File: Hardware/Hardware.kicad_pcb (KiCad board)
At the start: 2 copper layers, 39 parts, among them J2 RJ45_LED_Shielded, J3 USB_A, J5 Conn_01x06_Pin, SW1 SW_SPST, SW14 SW_Push, SW2 SW_Push, SW3 SW_Push, SW4 SW_Push, SW5 SW_Push, SW6 SW_Push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

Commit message: Added some traces
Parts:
- moved D14 15.7 mm to (249.4, 87.0)
- moved SW1 9.99 mm to (249.2, 101.1)
- moved Conn1 6.48 mm to (167.4, 78.4)
- moved R1 5.87 mm to (238.0, 101.6), turned to 180 degrees
- moved R9 3.01 mm to (223.1, 103.1)
- moved BT1 2.03 mm to (236.7, 132.5)
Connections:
- SW2 pad 1: +3.3V -> +3V3
- SW3 pad 1: +3.3V -> +3V3
- SW4 pad 1: +3.3V -> +3V3
- SW5 pad 1: +3.3V -> +3V3
- SW6 pad 1: +3.3V -> +3V3
- SW7 pad 1: +3.3V -> +3V3
- U7 pad 4: +3.3V -> +3V3
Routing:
- net +3V3: track 0.00 -> 238.6 mm, vias 0 -> 4
- net kp_button6: track 0.00 -> 95.8 mm, vias 0 -> 1
- net MISO: track 0.00 -> 73.1 mm, vias 0 -> 1
- net kp_button4: track 0.00 -> 70.7 mm, vias 0 -> 1
- net kp_button5: track 0.00 -> 69.5 mm, vias 0 -> 1
- net MOSI: track 0.00 -> 66.1 mm, vias 0 -> 1
- net +5V: track 0.00 -> 62.1 mm, vias 0 -> 1
- net kp_button3: track 0.00 -> 61.8 mm, vias 0 -> 1
- net T_CS: track 0.00 -> 61.5 mm
- net SCK: track 0.00 -> 51.8 mm, vias 0 -> 1
- net kp_button1: track 0.00 -> 50.3 mm, vias 0 -> 1
- net Rx+: track 0.00 -> 46.6 mm, vias 0 -> 1
- net Rx-: track 0.00 -> 46.6 mm, vias 0 -> 1
- net T_IRQ: track 0.00 -> 46.2 mm, vias 0 -> 1
- net LED: track 0.00 -> 44.9 mm
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- added copper zone on B.Cu, net GND
- added copper zone on F.Cu, net GND
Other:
- board outline added: 102.9 x 121.9 mm

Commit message: finished up the layout and cleaned up libraries
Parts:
- removed C7: 0.1uF, Capacitor_SMD:C_0603_1608Metric_Pad1.08x0.95mm_HandSolder
- removed C8: 1uF, Capacitor_SMD:C_0603_1608Metric_Pad1.08x0.95mm_HandSolder
- added C5: 4.7nF, Capacitor_SMD:C_0603_1608Metric_Pad1.08x0.95mm_HandSolder, F.Cu at (177.1, 74.2)
- added H1: MountingHole, MRDT_Drill_Holes:4_40_Hole, F.Cu at (241.0, 65.0)
- added H2: MountingHole, MRDT_Drill_Holes:4_40_Hole, F.Cu at (157.7, 65.0)
- added H3: MountingHole, MRDT_Drill_Holes:4_40_Hole, F.Cu at (241.0, 130.6)
- added H4: MountingHole, MRDT_Drill_Holes:4_40_Hole, F.Cu at (157.8, 130.5)
- added H5: MountingHole, MRDT_Drill_Holes:4_40_Hole, F.Cu at (166.9, 196.6)
- added H6: MountingHole, MRDT_Drill_Holes:4_40_Hole, F.Cu at (231.9, 196.6)
- C6: value 4.7nF -> 1uF
- D1: value D_Schottky -> D_Schottky_ZLLS500; footprint MRDT_Passives:SOT-23_Diode -> Tester:D_Schottky_ZLLS500
- D2: renamed from D15; value D_Schottky -> D_Schottky_ZLLS500; footprint MRDT_Passives:SOT-23_Diode -> Tester:D_Schottky_ZLLS500
- SW2, SW3, SW4, SW5, SW6, SW7: footprint Button_Switch_SMD:SW_SPST_TL3305A -> Tester:SW_SPST_TL3301
- U7: footprint sw_spst:DISPLAY_ILI9341_TOUCH_32 -> Tester:DISPLAY_ILI9341_TOUCH_32
- moved SW1 94.0 mm to (157.2, 81.6), turned to -90 degrees
- moved D3 92.5 mm to (157.5, 97.2), turned to -90 degrees
- moved R4 85.3 mm to (157.5, 93.3), turned to 90 degrees
- moved BT1 69.0 mm to (168.7, 121.4)
- moved R9 50.3 mm to (174.8, 116.8), turned to 90 degrees
- moved R8 47.9 mm to (177.2, 77.7), turned to 180 degrees
- moved SW2 42.6 mm to (170.2, 156.5), turned to 0 degrees
- moved SW7 38.6 mm to (225.3, 160.0), turned to 0 degrees
- moved C2 34.5 mm to (165.7, 111.5), turned to 180 degrees
- moved SW3 33.8 mm to (184.2, 164.1), turned to 0 degrees
- moved R2 32.1 mm to (182.8, 77.7)
- moved C3 31.1 mm to (170.1, 111.5)
- moved C4 28.4 mm to (182.9, 74.2), turned to 180 degrees
- moved SW4 28.1 mm to (207.5, 160.0), turned to 0 degrees
- moved C6 28.1 mm to (172.0, 116.8), turned to -90 degrees
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- renumbered D14 to D3, SW14 to SW8
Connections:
- net kp_button1 renamed KP_ACCEPT
- net kp_button2 renamed KP_BACK
- net kp_button3 renamed KP_RIGHT
- net kp_button6 renamed KP_LEFT
- C6 pad 1: Net-(C6-Pad1) -> WiFi_EN
- D1 pad 2: Net-(D1-A) -> unconnected-(D1-NC-Pad2)
- D1 pad 3: (no net) -> Net-(D1-A)
- D2 pad 2: Net-(D15-A) -> unconnected-(D2-NC-Pad2)
- D2 pad 3: (no net) -> Net-(D2-A)
- J3 pad 1: Net-(D15-A) -> Net-(D2-A)
- R8 pad 2: Net-(C6-Pad1) -> Net-(C5-Pad1)
- SW2 pad 1: +3V3 -> GND
- SW3 pad 1: +3V3 -> GND
- SW4 pad 1: +3V3 -> GND
- SW5 pad 1: +3V3 -> GND
- SW5 pad 2: kp_button4 -> KP_UP
- SW6 pad 1: +3V3 -> GND
- SW6 pad 2: kp_button5 -> KP_DOWN
- SW7 pad 1: +3V3 -> GND
- U3 pad 17: kp_button4 -> KP_DOWN
- U3 pad 18: kp_button5 -> KP_UP
- U3 pad 33: unconnected-(U3-MCLK2-Pad33) -> WiFi_EN
- U3 pad D-: (no net) -> USB_D-
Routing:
- net +5V: track 62.1 -> 167.5 mm, vias 1 -> 4
- net +3V3: track 238.6 -> 151.2 mm
- net KP_DOWN: track 0.00 -> 83.3 mm, vias 0 -> 1
- net Net-(D1-A): track 21.4 -> 96.8 mm
- net kp_button4: track 70.7 -> 0.00 mm, vias 1 -> 0
- net kp_button5: track 69.5 -> 0.00 mm, vias 1 -> 0
- net KP_UP: track 0.00 -> 68.2 mm, vias 0 -> 1
- net SCK: track 51.8 -> 94.6 mm, vias 1 -> 4
- net KP_ACCEPT: track 50.3 -> 91.2 mm
- net KP_BACK: track 43.9 -> 83.6 mm
- net WiFi_EN: track 34.1 -> 73.5 mm, vias 2 -> 0
- net MOSI: track 66.1 -> 104.3 mm, vias 1 -> 4
- net Net-(U2-CANH): track 17.0 -> 53.9 mm
- net Net-(U2-CANL): track 18.1 -> 52.8 mm
- net MISO: track 73.1 -> 96.9 mm, vias 1 -> 3
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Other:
- board size 102.9 x 121.9 mm -> 91.4 x 139.7 mm
- board text added: "Accept"
- board text added: "Back"

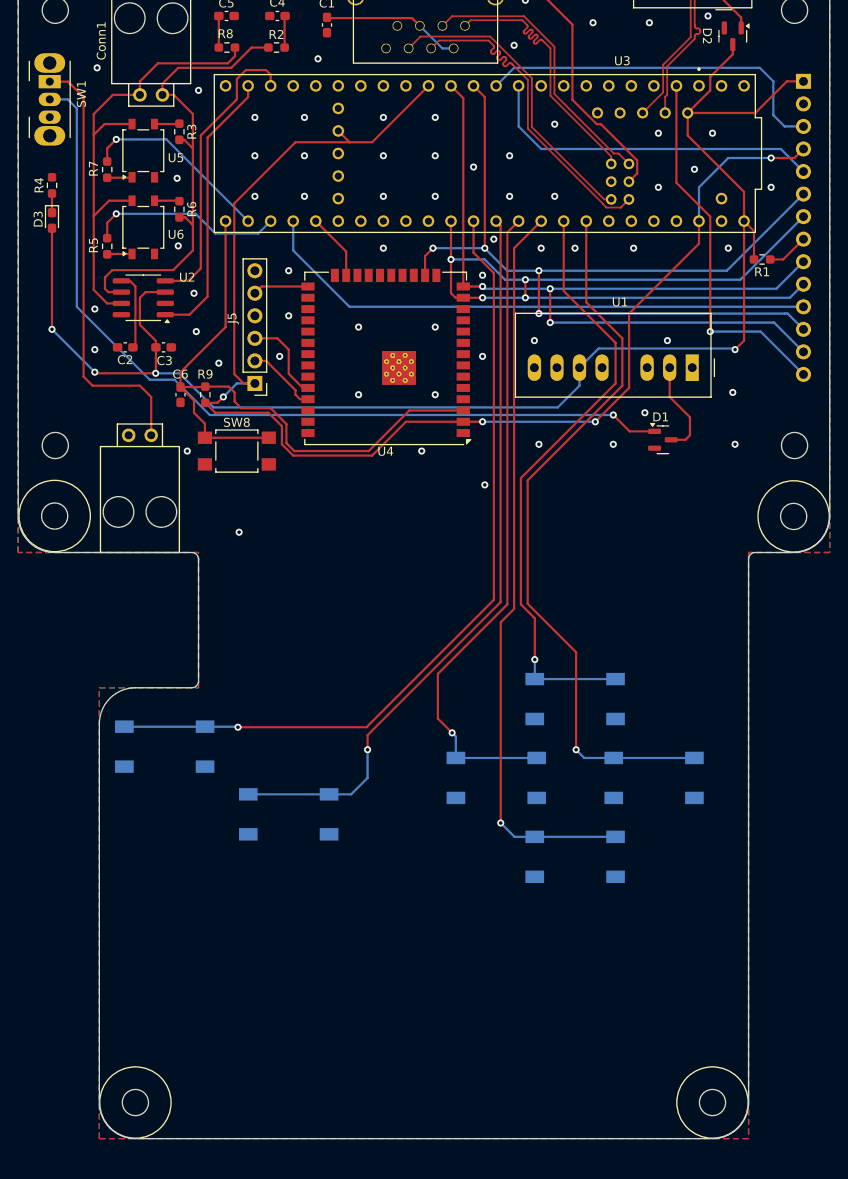
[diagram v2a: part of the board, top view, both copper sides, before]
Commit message: swapped buck and esp32 to make traces shorter
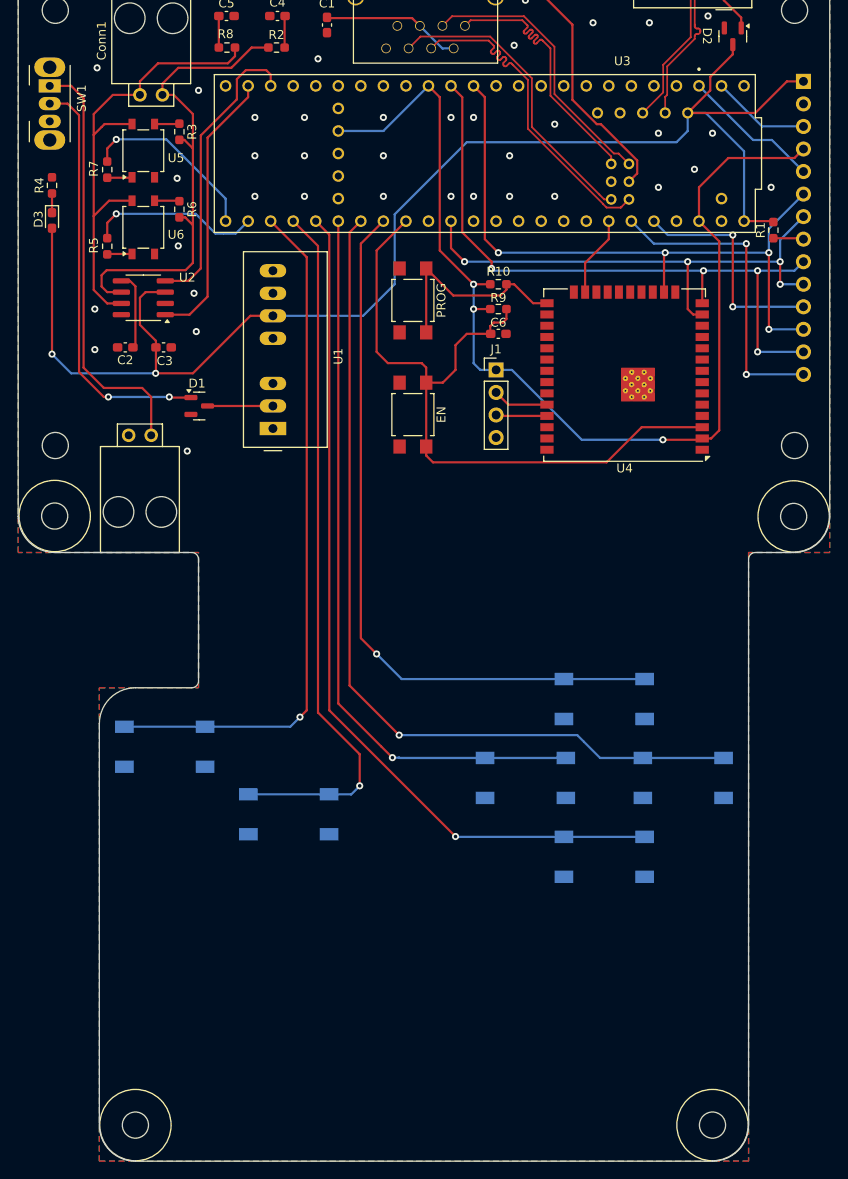
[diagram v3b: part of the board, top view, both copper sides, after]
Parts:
- removed J5: Conn_01x06_Pin, Connector_PinHeader_2.54mm:PinHeader_1x06_P2.54mm_Vertical
- added J1: Conn_01x04_Pin, Connector_PinHeader_2.54mm:PinHeader_1x04_P2.54mm_Vertical, F.Cu at (207.5, 114.0)
- added PROG: SW_Push, Button_Switch_SMD:SW_SPST_TL3305A, F.Cu at (198.1, 106.2)
- added R10: 10k, Resistor_SMD:R_0603_1608Metric_Pad0.98x0.95mm_HandSolder, F.Cu at (207.8, 104.4)
- moved D1 52.4 mm to (174.1, 118.1)
- moved U1 47.7 mm to (182.4, 120.7), turned to 90 degrees
- moved C6 36.5 mm to (207.8, 110.0), turned to 0 degrees
- moved R9 34.4 mm to (207.8, 107.2), turned to 0 degrees
- moved U4 27.0 mm to (222.0, 114.6)
- moved EN 20.3 mm to (198.1, 119.1), turned to -90 degrees
- moved R1 3.54 mm to (238.8, 98.3), turned to 90 degrees
- moved SW4 3.28 mm to (210.8, 160.0)
- moved SW5 3.28 mm to (219.7, 151.1)
- moved SW6 3.28 mm to (219.7, 168.9)
- moved SW7 3.28 mm to (228.6, 160.0)
- moved H5 2.54 mm to (166.9, 199.1)
- moved H6 2.54 mm to (231.9, 199.1)
- moved SW1 0.48 mm to (157.2, 82.0)
- renumbered SW8 to EN
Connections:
- U3 pad 0: unconnected-(U3-RX1-Pad0) -> LCD_CS
- U3 pad 1: unconnected-(U3-TX1-Pad1) -> DC
- U3 pad 10: LCD_CS -> unconnected-(U3-CS1-Pad10)
- U3 pad 14: KP_ACCEPT -> unconnected-(U3-A0-Pad14)
- U3 pad 15: KP_BACK -> unconnected-(U3-A1-Pad15)
- U3 pad 16: KP_RIGHT -> unconnected-(U3-A2-Pad16)
- U3 pad 17: KP_DOWN -> unconnected-(U3-A3-Pad17)
- U3 pad 18: KP_UP -> unconnected-(U3-A4-Pad18)
- U3 pad 19: KP_LEFT -> unconnected-(U3-A5-Pad19)
- U3 pad 2: T_IRQ -> unconnected-(U3-OUT2-Pad2)
- U3 pad 20: unconnected-(U3-A6-Pad20) -> WiFi_CS
- U3 pad 21: unconnected-(U3-A7-Pad21) -> T_IRQ
- U3 pad 22: unconnected-(U3-A8-Pad22) -> T_CS
- U3 pad 33: WiFi_EN -> R1_EN
- U3 pad 34: R1_EN -> R2_EN
- U3 pad 35: R2_EN -> KP_ACCEPT
- U3 pad 36: T_CS -> KP_BACK
- U3 pad 37: WiFi_CS -> KP_DOWN
- U3 pad 38: unconnected-(U3-A14-Pad38) -> KP_RIGHT
- U3 pad 39: unconnected-(U3-A15-Pad39) -> KP_LEFT
- U3 pad 40: unconnected-(U3-A16-Pad40) -> KP_UP
- U3 pad 41: unconnected-(U3-A17-Pad41) -> WiFi_EN
- U3 pad 9: DC -> unconnected-(U3-OUT1C-Pad9)
- U4 pad 25: BOOT -> PROG
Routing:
- net Net-(D1-A): track 96.8 -> 47.1 mm, vias 1 -> 2
- net T_CS: track 63.4 -> 25.6 mm, vias 0 -> 2
- net SCK: track 94.6 -> 59.6 mm
- net LCD_CS: track 40.4 -> 11.1 mm
- net MOSI: track 104.3 -> 75.9 mm
- net +3V3: track 151.2 -> 123.2 mm, vias 4 -> 3
- net PROG: track 0.00 -> 23.8 mm
- net DC: track 38.8 -> 15.8 mm
- net MISO: track 96.9 -> 76.4 mm, vias 3 -> 4
- net KP_LEFT: track 81.6 -> 98.4 mm
- net KP_DOWN: track 83.3 -> 97.2 mm
- net KP_UP: track 68.2 -> 81.9 mm
- net KP_ACCEPT: track 91.2 -> 78.1 mm
- net KP_RIGHT: track 74.2 -> 82.5 mm
- net WiFi_EN: track 73.5 -> 80.7 mm
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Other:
- board size 91.4 x 139.7 mm -> 91.4 x 142.2 mm
